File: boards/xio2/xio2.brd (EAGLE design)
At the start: 170 x 100 mm, 379 parts, among them J1 12401598E4#2A, Q1 BSS138, Q2 BSS138, Q3 BC817-16LT3G, Q4 BC817-16LT3G, Y2 FA-238 25.0000MB-K3

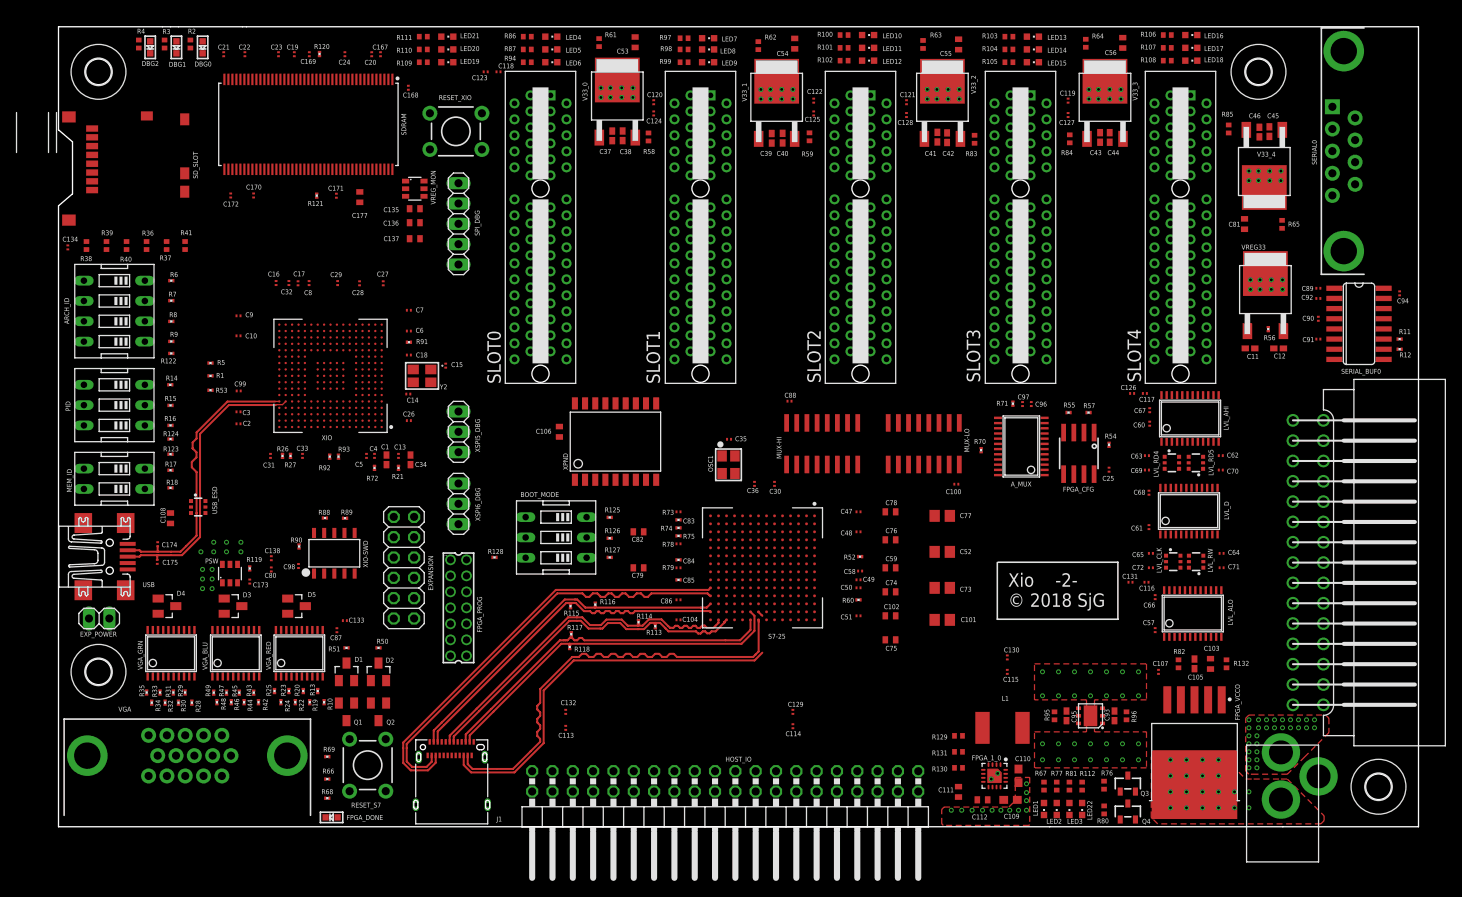
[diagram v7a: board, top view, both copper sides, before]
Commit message: Routed board. SDRAM has a long line…
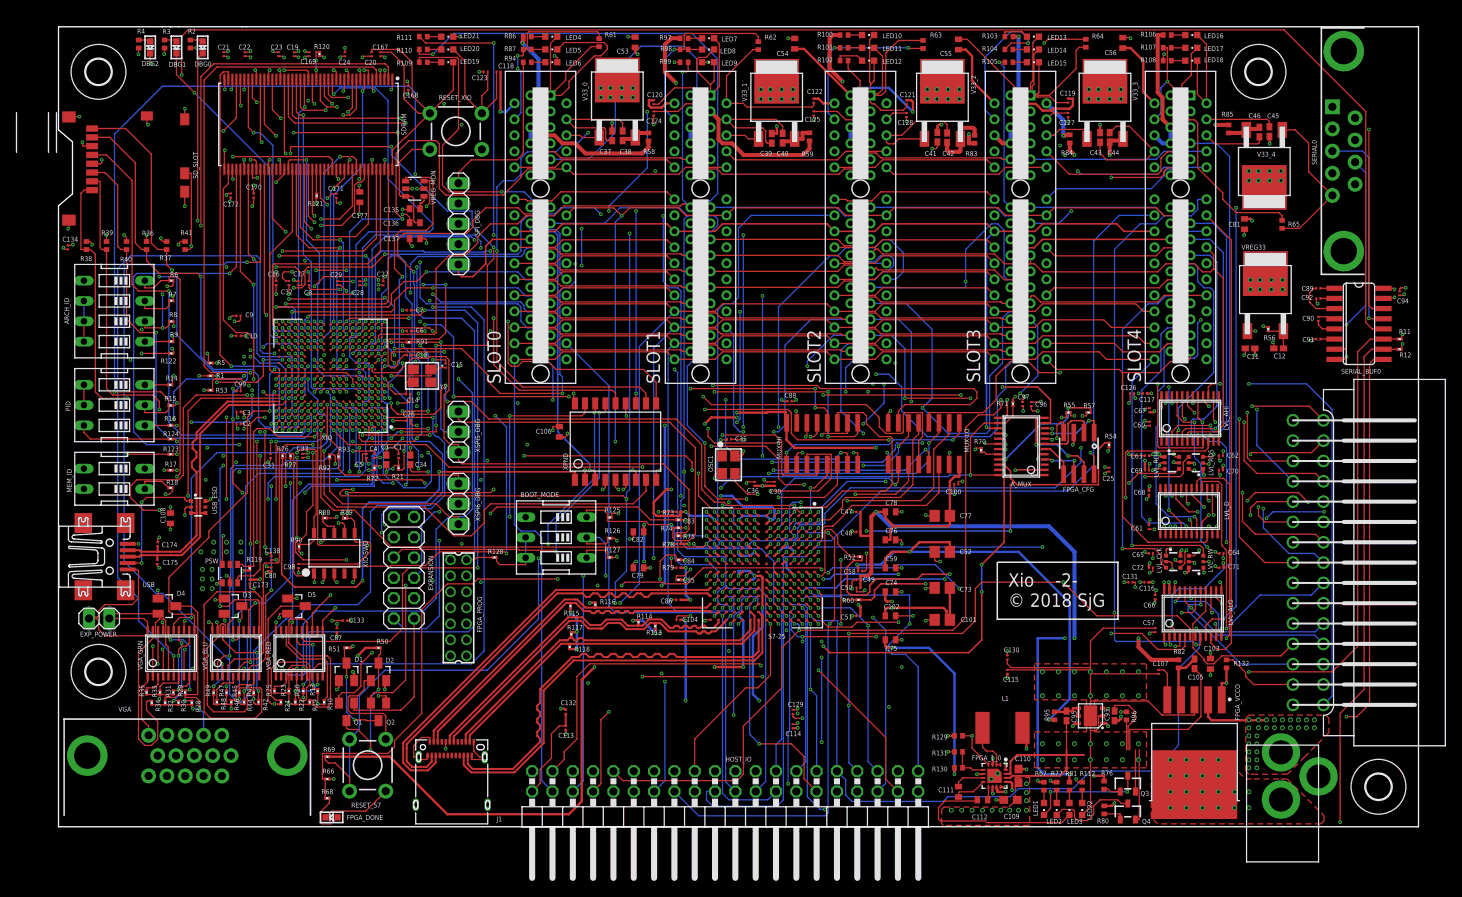
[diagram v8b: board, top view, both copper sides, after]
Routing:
- net GND: track 0.00 -> 931.5 mm, vias 62 -> 358
- net VCCO: track 0.00 -> 356.3 mm, vias 0 -> 35
- net HOST_A4: track 0.00 -> 343.8 mm, vias 0 -> 4
- net HOST_A3: track 0.00 -> 318.4 mm, vias 0 -> 9
- net HOST_A1: track 0.00 -> 301.8 mm, vias 0 -> 5
- net HOST_A7: track 0.00 -> 283.2 mm, vias 0 -> 7
- net HOST_A0: track 0.00 -> 280.7 mm, vias 0 -> 5
- net HOST_A9: track 0.00 -> 278.3 mm, vias 0 -> 7
- net HOST_A5: track 0.00 -> 276.6 mm, vias 0 -> 7
- net HOST_A6: track 0.00 -> 271.4 mm, vias 0 -> 10
- net HOST_A12: track 0.00 -> 269.0 mm, vias 0 -> 9
- net HOST_A2: track 0.00 -> 266.5 mm, vias 0 -> 6
- net HOST_A8: track 0.00 -> 265.0 mm, vias 0 -> 9
- net HOST_A10: track 0.00 -> 263.9 mm, vias 0 -> 10
- net HOST_A11: track 0.00 -> 259.5 mm, vias 0 -> 10
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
